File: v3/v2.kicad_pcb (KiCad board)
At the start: 2 copper layers, 178.7 x 150.8 mm, 122 parts, among them J2 Conn_01x04_Pin, J3 Conn_01x04_Pin, SW1 SW_Push, SW10 SW_Push, SW11 SW_Push, SW12 SW_Push, SW13 SW_Push, SW14 SW_Push, SW15 SW_Push, SW16 SW_Push, SW17 SW_Push, SW18 SW_Push, SW19 SW_Push, SW2 SW_Push, SW20 SW_Push, SW21 SW_Push, SW22 SW_Push, SW23 SW_Push, SW24 SW_Push, SW25 SW_Push, SW26 SW_Push, SW27 SW_Push, SW28 SW_Push, SW29 SW_Push, SW3 SW_Push, SW30 SW_Push, SW31 SW_Push, SW32 SW_Push, SW33 RotaryEncoder_Switch, SW4 SW_Push, SW5 SW_Push, SW6 SW_Push, SW7 SW_Push, SW8 SW_Push, SW9 SW_Push, U1 Pico, U2 Pico

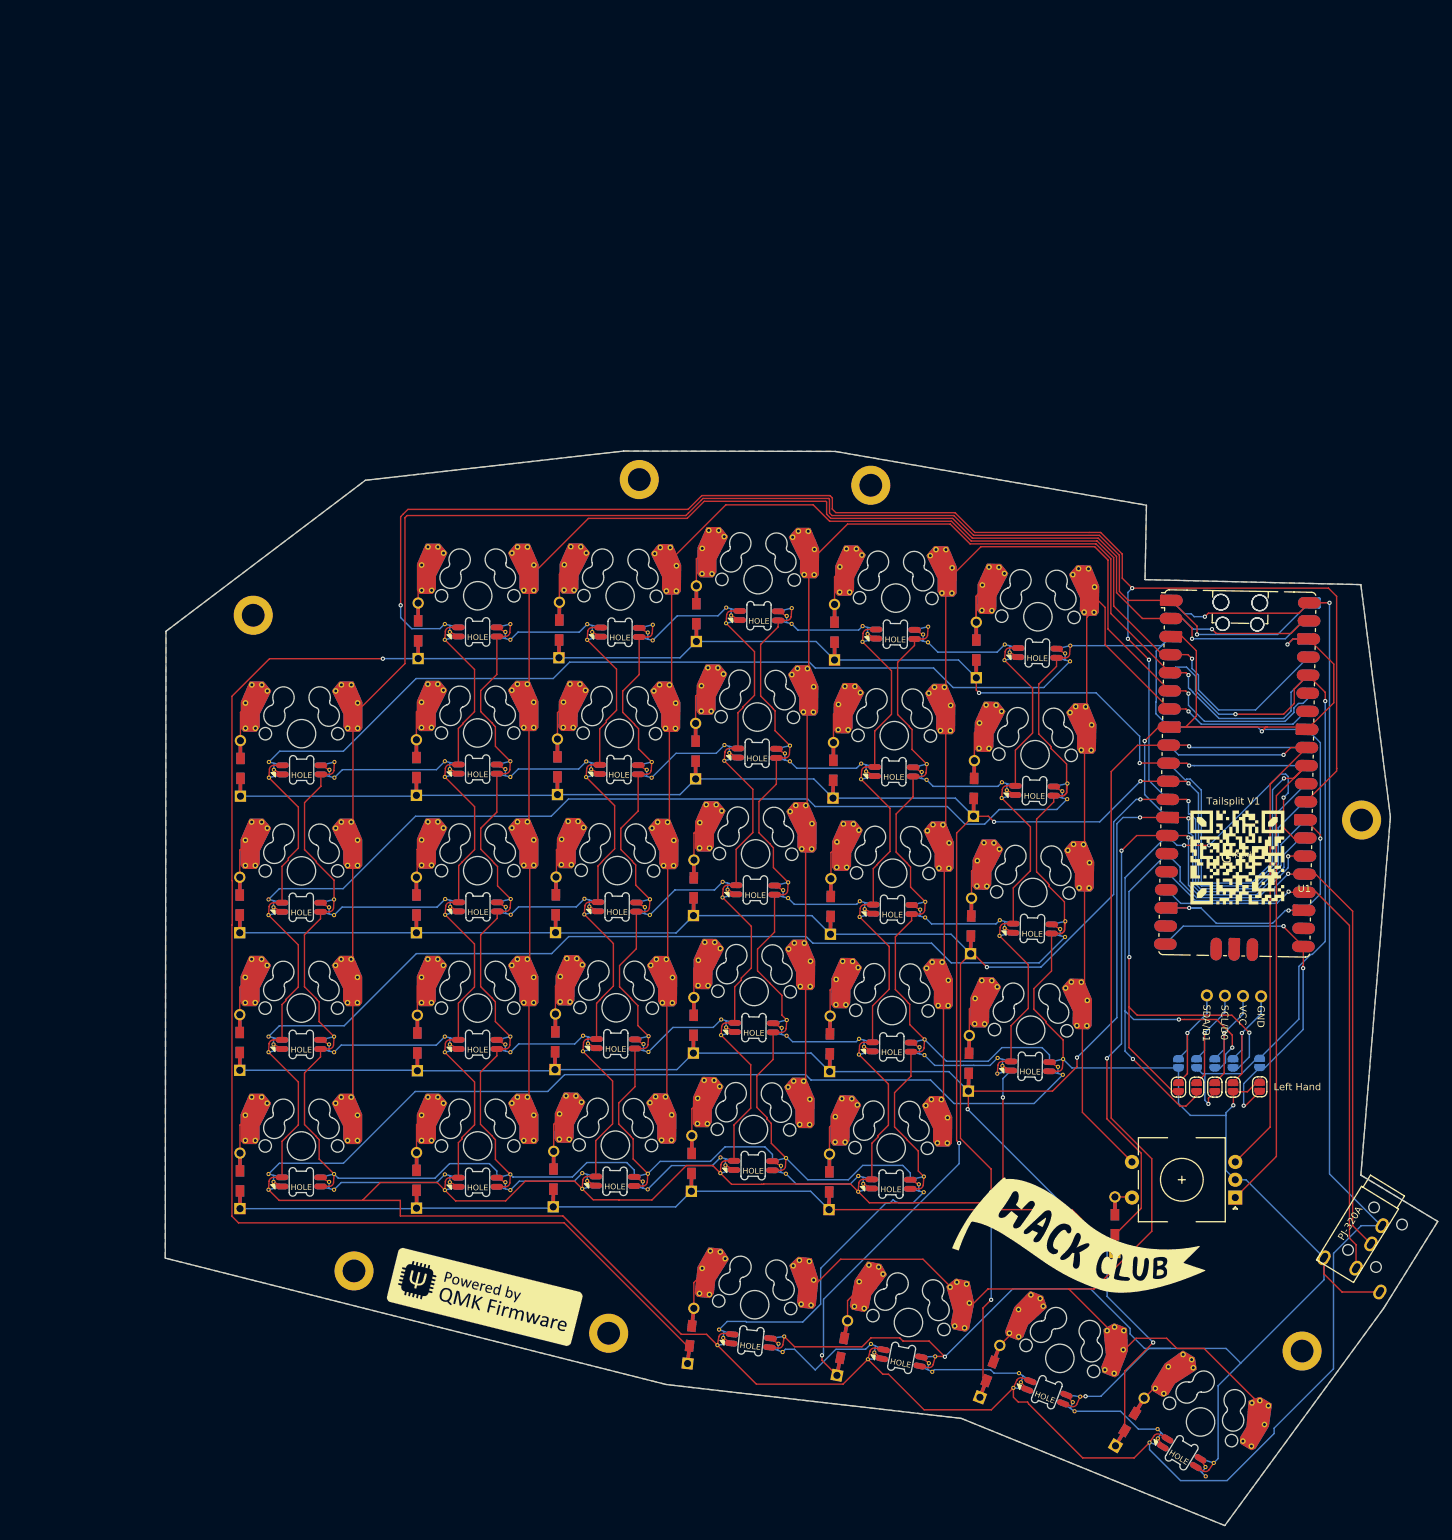
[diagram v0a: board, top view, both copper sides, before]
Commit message: redid footprints and layout for pcb
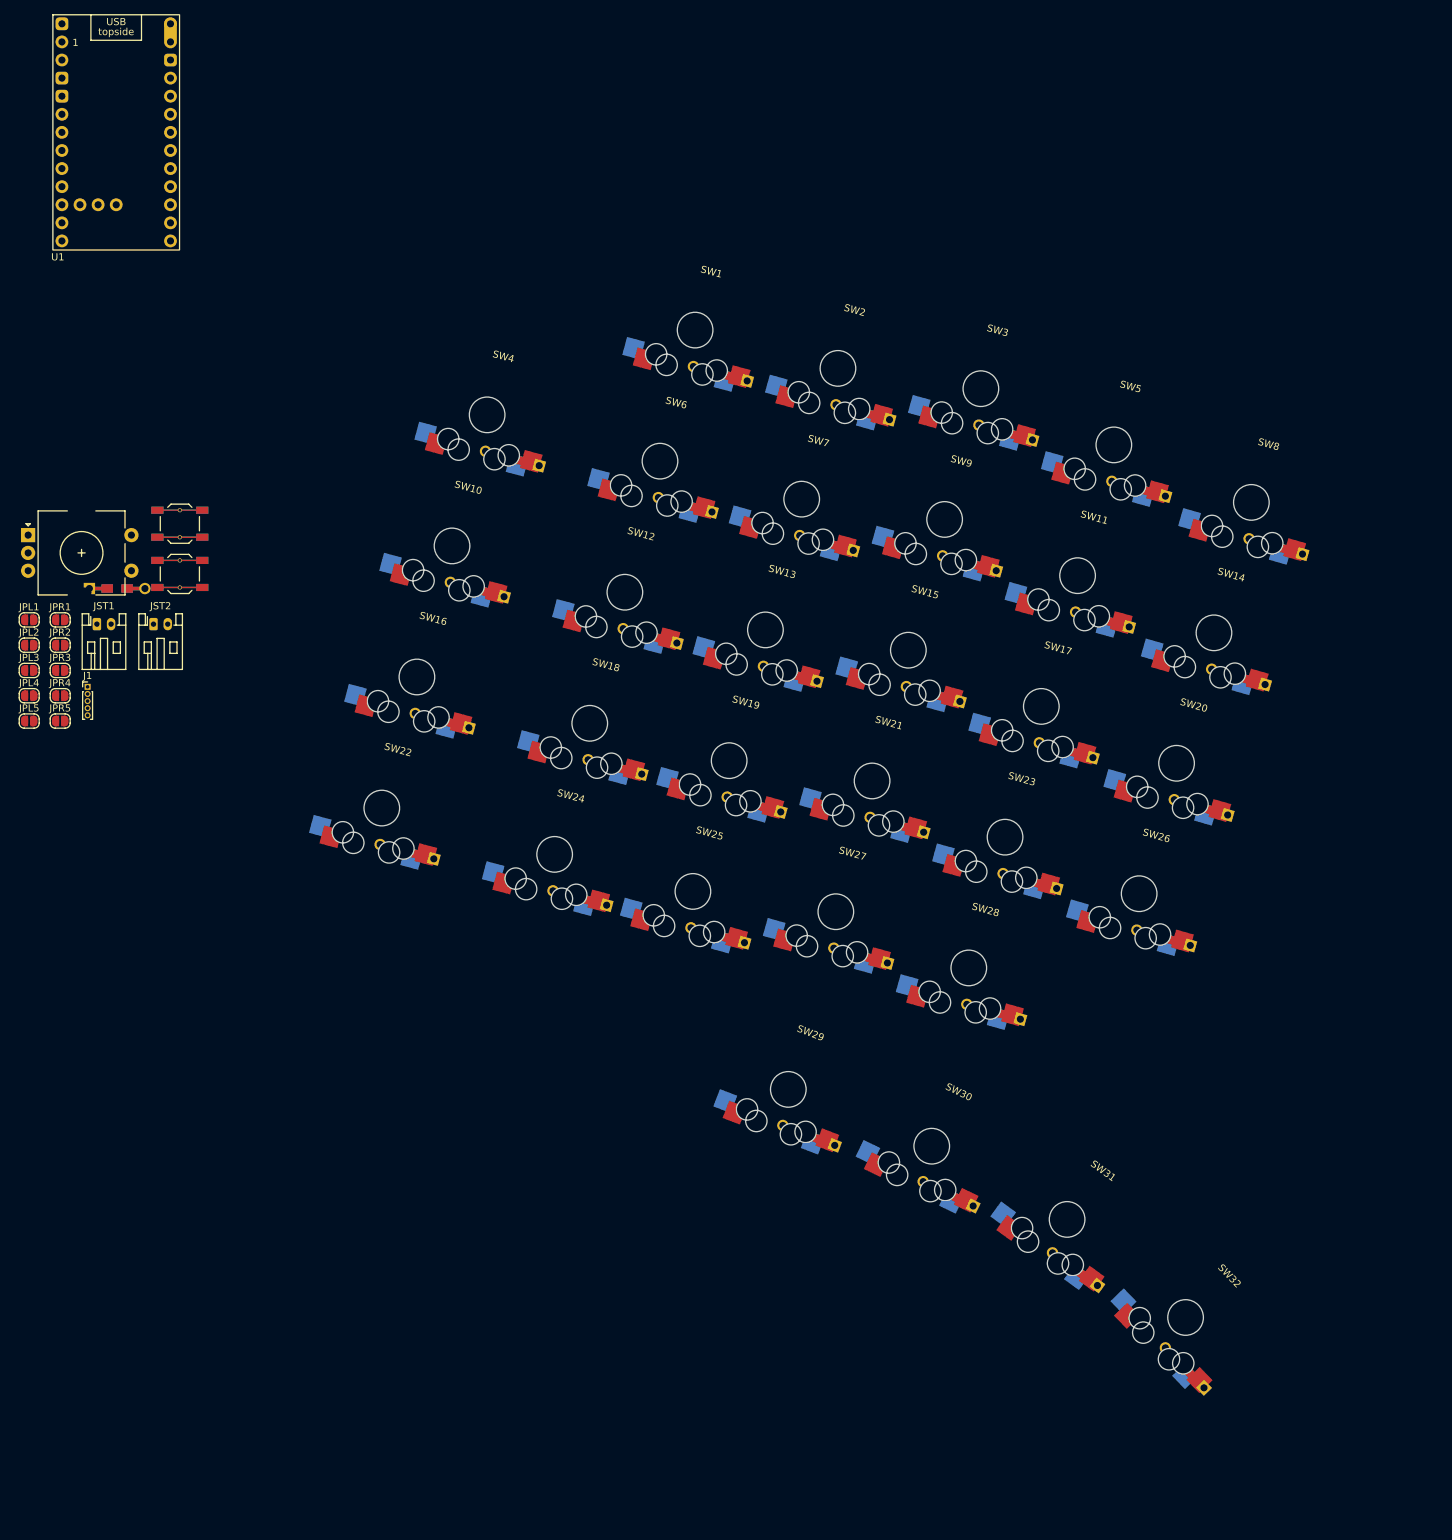
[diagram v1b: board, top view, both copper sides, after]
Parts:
- removed G*** (x2): LOGO, footprints:QMK_PoweredBy
- removed G***: LOGO, LOGO
- removed J2: Conn_01x04_Pin, Keebio-Parts:I2C_Breakout
- removed J3: Conn_01x04_Pin, Keebio-Parts:TRRS-PJ-320A-dual
- removed JP1, JP8: GND, Jumper:SolderJumper-2_P1.3mm_Open_RoundedPad1.0x1.5mm
- removed JP10: Left, Jumper:SolderJumper-2_P1.3mm_Open_RoundedPad1.0x1.5mm
- removed JP2, JP7: VCC, Jumper:SolderJumper-2_P1.3mm_Open_RoundedPad1.0x1.5mm
- removed JP3, JP6: SCL, Jumper:SolderJumper-2_P1.3mm_Open_RoundedPad1.0x1.5mm
- removed JP4, JP5: SDA, Jumper:SolderJumper-2_P1.3mm_Open_RoundedPad1.0x1.5mm
- removed JP9: Right, Jumper:SolderJumper-2_P1.3mm_Open_RoundedPad1.0x1.5mm
- removed LED1, LED10, LED11, LED12, LED13, LED14, LED15, LED16, LED17, LED18, LED19, LED2, LED20, LED21, LED22, LED23, LED24, LED25, LED26, LED27, LED28, LED29, LED3, LED30, LED31, LED32, LED4, LED5, LED6, LED7, LED8, LED9: SK6812MINI, reversible-kicad-footprints:MX-1U-SK6812Mini-E
- removed REF** (x7): MountingHole_3.2mm_M3_ISO14580_Pad, Keebio-Parts:MountingHole_3.2mm_M3_ISO14580_Pad
- removed U2: Pico, Module:RaspberryPi_Pico_SMD_HandSolder
- added J1: Conn_01x05_Pin, Connector_PinHeader_1.00mm:PinHeader_1x05_P1.00mm_Vertical, F.Cu at (96.2, 109.8)
- added JPL1: SolderJumper_2_Open, Jumper:SolderJumper-2_P1.3mm_Open_RoundedPad1.0x1.5mm, F.Cu at (88.0, 100.5)
- added JPL2: SolderJumper_2_Open, Jumper:SolderJumper-2_P1.3mm_Open_RoundedPad1.0x1.5mm, F.Cu at (88.0, 104.0)
- added JPL3: SolderJumper_2_Open, Jumper:SolderJumper-2_P1.3mm_Open_RoundedPad1.0x1.5mm, F.Cu at (88.0, 107.5)
- added JPL4: SolderJumper_2_Open, Jumper:SolderJumper-2_P1.3mm_Open_RoundedPad1.0x1.5mm, F.Cu at (88.0, 111.1)
- added JPL5: SolderJumper_2_Open, Jumper:SolderJumper-2_P1.3mm_Open_RoundedPad1.0x1.5mm, F.Cu at (88.0, 114.7)
- added JPR1: SolderJumper_2_Open, Jumper:SolderJumper-2_P1.3mm_Open_RoundedPad1.0x1.5mm, F.Cu at (92.4, 100.5)
- added JPR2: SolderJumper_2_Open, Jumper:SolderJumper-2_P1.3mm_Open_RoundedPad1.0x1.5mm, F.Cu at (92.4, 104.0)
- added JPR3: SolderJumper_2_Open, Jumper:SolderJumper-2_P1.3mm_Open_RoundedPad1.0x1.5mm, F.Cu at (92.4, 107.5)
- added JPR4: SolderJumper_2_Open, Jumper:SolderJumper-2_P1.3mm_Open_RoundedPad1.0x1.5mm, F.Cu at (92.4, 111.1)
- added JPR5: SolderJumper_2_Open, Jumper:SolderJumper-2_P1.3mm_Open_RoundedPad1.0x1.5mm, F.Cu at (92.4, 114.7)
- added JST1: Conn_01x02_Pin, Connector_JST:JST_PH_S2B-PH-K_1x02_P2.00mm_Horizontal, F.Cu at (97.5, 101.0)
- added JST2: Conn_01x02_Pin, Connector_JST:JST_PH_S2B-PH-K_1x02_P2.00mm_Horizontal, F.Cu at (105.5, 101.0)
- added PWR1: SW_Push_45deg, reversible-kicad-footprints:SMD_Push, F.Cu at (109.2, 87.0)
- added RST1: SW_Push_45deg, reversible-kicad-footprints:SMD_Push, F.Cu at (109.2, 94.0)
- D1, D10, D11, D12, D13, D14, D15, D16, D17, D18, D19, D2, D20, D21, D22, D23, D24, D25, D26, D27, D28, D29, D3, D30, D31, D32, D33, D4, D5, D6, D7, D8, D9: footprint Keebio-Parts:Diode-Hybrid-Dual -> footprints:Diode-dual; moved to B.Cu
- SW1, SW10, SW11, SW12, SW13, SW14, SW15, SW16, SW17, SW18, SW19, SW2, SW20, SW21, SW22, SW23, SW24, SW25, SW26, SW27, SW28, SW29, SW3, SW30, SW31, SW32, SW4, SW5, SW6, SW7, SW8, SW9: footprint reversible-kicad-footprints:MX-1U-Hotswap -> footprints:gateron-ks27-hotswap-reversible
- SW33: footprint Keebio-Parts:RotaryEncoder_EC11 -> Keebio-Parts.pretty-master:RotaryEncoder_EC11
- U1: value Pico -> nice_nano; footprint Module:RaspberryPi_Pico_SMD_HandSolder -> PCM_marbastlib-xp-promicroish:nice_nano_AH_USBup
- moved U1 180.7 mm to (100.3, 33.3), turned to 0 degrees
- moved SW33 177.8 mm to (95.4, 91.0), turned to 0 degrees
- moved D8 153.9 mm to (263.1, 90.1), turned to -16 degrees
- moved SW8 143.0 mm to (259.6, 84.0), turned to -16 degrees
- moved SW7 113.3 mm to (196.5, 83.5), turned to -15.5 degrees
- moved D7 112.9 mm to (200.0, 89.7), turned to -15.5 degrees
- moved D14 109.4 mm to (257.8, 108.5), turned to -16 degrees
- moved D15 108.9 mm to (215.0, 110.9), turned to -15.5 degrees
- moved SW14 105.9 mm to (254.4, 102.3), turned to -16 degrees
- moved SW15 98.9 mm to (211.5, 104.7), turned to -15.5 degrees
- moved D29 93.1 mm to (100.4, 96.0), turned to 180 degrees
- moved D23 88.9 mm to (228.5, 137.1), turned to -15.5 degrees
- moved D1 87.2 mm to (185.1, 65.9), turned to -15 degrees
- moved SW21 85.2 mm to (206.4, 123.1), turned to -15.5 degrees
- moved D9 82.8 mm to (220.0, 92.5), turned to -15.5 degrees
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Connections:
- D1 pad 1: Row 2 -> Row 1
- D12 pad 1: Row 2 -> Row 3
- D13 pad 1: Row 2 -> Row 3
- D14 pad 1: Row 2 -> Row 3
- D15 pad 1: Row 4 -> Row 3
- D18 pad 1: Row 3 -> Row 4
- D19 pad 1: Row 3 -> Row 4
- D20 pad 1: Row 3 -> Row 4
- D21 pad 1: Row 3 -> Row 4
- D22 pad 1: Row 5 -> Row 4
- D24 pad 1: Row 4 -> Row 5
- D25 pad 1: Row 4 -> Row 5
- D26 pad 1: Row 4 -> Row 5
- D27 pad 1: Row 4 -> Row 5
- D28 pad 1: Row 4 -> Row 5
- D29 pad 2: Net-(D29-A) -> ENCSWB
- D30 pad 1: Row 5 -> Row 6
- D31 pad 1: Row 5 -> Row 6
- D32 pad 1: Row 5 -> Row 6
- D33 pad 1: Row 5 -> Row 6
- D33 pad 2: ENCSWB -> Net-(D33-A)
- D6 pad 1: Row 1 -> Row 2
- D7 pad 1: Row 1 -> Row 2
- D8 pad 1: Row 3 -> Row 2
- SW1 pad 2: Col 1 -> Col 2
- SW10 pad 2: Col 3 -> Col 5
- SW11 pad 2: Col 4 -> Col 6
- SW12 pad 2: Col 5 -> Col 1
- SW13 pad 2: Col 6 -> Col 2
- SW14 pad 2: Col 7 -> Col 3
- SW15 pad 2: Col 1 -> Col 4
- SW16 pad 2: Col 2 -> Col 5
- SW17 pad 2: Col 3 -> Col 6
- SW18 pad 2: Col 4 -> Col 1
- SW19 pad 2: Col 5 -> Col 2
- SW2 pad 2: Col 2 -> Col 3
- SW20 pad 2: Col 6 -> Col 3
- SW21 pad 2: Col 7 -> Col 4
- SW22 pad 2: Col 1 -> Col 5
- SW23 pad 2: Col 2 -> Col 6
- SW24 pad 2: Col 3 -> Col 1
- SW25 pad 2: Col 4 -> Col 2
- SW26 pad 2: Col 5 -> Col 3
- SW27 pad 2: Col 6 -> Col 4
- SW28 pad 2: Col 7 -> Col 5
- SW29 pad 1: Net-(D29-A) -> Net-(D30-A)
- SW29 pad 2: Col 2 -> Col 1
- SW3 pad 2: Col 3 -> Col 4
- SW30 pad 1: Net-(D30-A) -> Net-(D31-A)
- SW30 pad 2: Col 3 -> Col 2
- SW31 pad 1: Net-(D31-A) -> Net-(D32-A)
- SW31 pad 2: Col 4 -> Col 3
- SW32 pad 1: Net-(D32-A) -> Net-(D33-A)
- SW32 pad 2: Col 5 -> Col 4
- SW4 pad 2: Col 4 -> Col 5
- SW5 pad 2: Col 5 -> Col 6
- SW6 pad 2: Col 6 -> Col 1
- SW7 pad 2: Col 7 -> Col 2
- SW8 pad 2: Col 1 -> Col 3
- SW9 pad 2: Col 2 -> Col 4
- U1 pad 1: Col 1 -> unconnected-(U1-P0.06-Pad1)
- U1 pad 10: Row 1 -> unconnected-(U1-P0.11-Pad10)
- U1 pad 11: Row 2 -> unconnected-(U1-P1.04-LF-Pad11)
- U1 pad 12: Row 3 -> unconnected-(U1-P1.06-LF-Pad12)
- U1 pad 13: Row 4 -> unconnected-(U1-BAT+-Pad13)
- U1 pad 14: Row 5 -> unconnected-(U1-GND-Pad14)
- U1 pad 18: GND -> unconnected-(U1-P0.29-LF-Pad18)
- U1 pad 2: Col 2 -> unconnected-(U1-P0.08-Pad2)
- U1 pad 21: SPLIT SELECT -> unconnected-(U1-P1.13-LF-Pad21)
- U1 pad 23: GND -> unconnected-(U1-P0.10-LF-Pad23)
- U1 pad 24: SERIAL B -> unconnected-(U1-P0.09-LF-Pad24)
- U1 pad 25: SERIAL A -> unconnected-(U1-P1.01-LF-Pad25)
- U1 pad 26: SDA -> unconnected-(U1-P1.02-LF-Pad26)
- U1 pad 27: SDL -> unconnected-(U1-P1.07-LF-Pad27)
- U1 pad 28: GND -> unconnected-(U1-GND-Pad28)
- U1 pad 29: SK6912PWM -> unconnected-(U1-BAT+-Pad29)
- U1 pad 3: GND -> unconnected-(U1-GND-Pad3)
- U1 pad 4: Col 3 -> unconnected-(U1-GND-Pad4)
- U1 pad 5: Col 4 -> unconnected-(U1-P0.17-Pad5)
- U1 pad 6: Col 5 -> unconnected-(U1-P0.20-Pad6)
- U1 pad 7: Col 6 -> unconnected-(U1-P0.22-Pad7)
- U1 pad 8: GND -> unconnected-(U1-P0.24-Pad8)
- U1 pad 9: Col 7 -> unconnected-(U1-P1.00-Pad9)
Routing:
- net GND: track 943.5 -> 0.00 mm, vias 9 -> 0
- net VBUS: track 883.7 -> 0.00 mm, vias 3 -> 0
- net Row 1: track 309.3 -> 0.00 mm, vias 4 -> 0
- net Row 2: track 267.3 -> 0.00 mm, vias 5 -> 0
- net Row 4: track 261.2 -> 0.00 mm, vias 5 -> 0
- net Row 3: track 252.0 -> 0.00 mm, vias 5 -> 0
- net Col 1: track 231.3 -> 0.00 mm, vias 1 -> 0
- net SK6912PWM: track 225.6 -> 0.00 mm, vias 4 -> 0
- net Row 5: track 224.1 -> 0.00 mm, vias 3 -> 0
- net Col 2: track 205.2 -> 0.00 mm, vias 1 -> 0
- net Col 7: track 197.5 -> 0.00 mm, vias 1 -> 0
- net Col 3: track 192.1 -> 0.00 mm, vias 1 -> 0
- net Col 4: track 170.6 -> 0.00 mm, vias 1 -> 0
- net Col 5: track 149.3 -> 0.00 mm, vias 1 -> 0
- net Col 6: track 123.9 -> 0.00 mm, vias 1 -> 0
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- removed copper zone on B.Cu, net GND
- removed copper zone on F.Cu, net GND
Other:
- board outline removed
- board text removed: "Left Hand"
- board text removed: "Right Hand"
- board text removed: "Tailsplit V1"

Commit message: start placing switches
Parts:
- J1: footprint Connector_PinHeader_1.00mm:PinHeader_1x05_P1.00mm_Vertical -> Connector_PinHeader_2.54mm:PinHeader_1x05_P2.54mm_Vertical
- PWR1, RST1: footprint reversible-kicad-footprints:SMD_Push -> footprints:EVQ-P7C-Reversible
- moved D16 76.2 mm to (149.1, 190.7)
- moved D10 76.2 mm to (154.0, 172.3)
- moved D18 76.2 mm to (173.4, 197.2)
- moved D22 76.2 mm to (144.2, 209.1)
- moved D24 76.2 mm to (168.4, 215.6)
- moved D6 76.2 mm to (183.2, 160.4)
- moved D1 76.2 mm to (188.2, 142.0)
- moved D12 76.2 mm to (178.3, 178.8)
- moved D4 76.2 mm to (159.0, 153.9)
- moved D13 76.2 mm to (198.0, 184.1)
- moved D15 76.2 mm to (218.0, 187.0)
- moved D17 76.2 mm to (236.7, 194.9)
- moved D19 76.2 mm to (192.9, 202.5)
- moved D23 76.2 mm to (231.6, 213.2)
- moved D25 76.2 mm to (187.8, 220.8)
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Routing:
- net Net-(D31-A): track 0.00 -> 3.87 mm
- net Net-(D15-A): track 0.00 -> 3.87 mm
- net Net-(D9-A): track 0.00 -> 3.87 mm
- net Net-(D5-A): track 0.00 -> 3.87 mm
- net Net-(D3-A): track 0.00 -> 3.87 mm
- net Net-(D2-A): track 0.00 -> 3.87 mm
- net Net-(D32-A): track 0.00 -> 3.87 mm
- net Net-(D33-A): track 0.00 -> 3.87 mm
- net Net-(D23-A): track 0.00 -> 3.87 mm
- net Net-(D17-A): track 0.00 -> 3.87 mm
- net Net-(D21-A): track 0.00 -> 3.87 mm
- net Net-(D19-A): track 0.00 -> 3.87 mm
- net Net-(D28-A): track 0.00 -> 3.87 mm
- net Net-(D7-A): track 0.00 -> 3.87 mm
- net Net-(D27-A): track 0.00 -> 3.87 mm
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
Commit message: grid sizing right and other fun stuff
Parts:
- D1, D10, D11, D12, D13, D14, D15, D16, D17, D18, D19, D2, D20, D21, D22, D23, D24, D25, D26, D27, D28, D29, D3, D30, D31, D32, D33, D4, D5, D6, D7, D8, D9: moved to F.Cu
- moved SW8 248.8 mm to (20.9, 134.0), turned to 0 degrees
- moved SW26 247.6 mm to (77.8, 37.4), turned to 0 degrees
- moved SW17 244.3 mm to (58.9, 21.3), turned to 0 degrees
- moved D33 242.1 mm to (113.3, 80.4), turned to 0 degrees
- moved SW5 237.1 mm to (20.9, 85.7), turned to 0 degrees
- moved SW14 235.4 mm to (39.9, 101.8), turned to 0 degrees
- moved SW20 235.0 mm to (58.9, 69.6), turned to 0 degrees
- moved SW11 234.1 mm to (39.9, 53.5), turned to 0 degrees
- moved SW9 231.7 mm to (39.9, 21.3), turned to 0 degrees
- moved SW32 228.0 mm to (77.8, 134.0), turned to 0 degrees
- moved D32 225.1 mm to (113.3, 77.7), turned to 0 degrees
- moved SW25 221.5 mm to (77.8, 21.3), turned to 0 degrees
- moved SW31 216.5 mm to (77.8, 117.9), turned to 0 degrees
- moved SW28 215.3 mm to (77.8, 69.6), turned to 0 degrees
- moved D26 210.3 mm to (113.3, 61.7), turned to 0 degrees
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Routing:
- net Net-(D31-A): track 3.87 -> 0.00 mm
- net Net-(D15-A): track 3.87 -> 0.00 mm
- net Net-(D9-A): track 3.87 -> 0.00 mm
- net Net-(D5-A): track 3.87 -> 0.00 mm
- net Net-(D3-A): track 3.87 -> 0.00 mm
- net Net-(D2-A): track 3.87 -> 0.00 mm
- net Net-(D32-A): track 3.87 -> 0.00 mm
- net Net-(D33-A): track 3.87 -> 0.00 mm
- net Net-(D23-A): track 3.87 -> 0.00 mm
- net Net-(D17-A): track 3.87 -> 0.00 mm
- net Net-(D21-A): track 3.87 -> 0.00 mm
- net Net-(D19-A): track 3.87 -> 0.00 mm
- net Net-(D28-A): track 3.87 -> 0.00 mm
- net Net-(D7-A): track 3.87 -> 0.00 mm
- net Net-(D27-A): track 3.87 -> 0.00 mm
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
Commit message: added all needed labels
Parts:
- added U2: nice_nano_right, PCM_marbastlib-xp-promicroish:nice_nano_AH_USBup, B.Cu at (2.52, 33.9)
- U1: value nice_nano -> nice_nano_left
- moved SW5 227.4 mm to (246.1, 53.7), turned to -0.9 degrees
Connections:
- U1 pad 1: unconnected-(U1-P0.06-Pad1) -> CS
- U1 pad 10: unconnected-(U1-P0.11-Pad10) -> Col 5
- U1 pad 11: unconnected-(U1-P1.04-LF-Pad11) -> Col 6
- U1 pad 12: unconnected-(U1-P1.06-LF-Pad12) -> ENC A
- U1 pad 13: unconnected-(U1-BAT+-Pad13) -> +BATT
- U1 pad 14: unconnected-(U1-GND-Pad14) -> GND
- U1 pad 15: unconnected-(U1-RST-Pad15) -> RST
- U1 pad 16: unconnected-(U1-3V3-Pad16) -> +3.3V
- U1 pad 17: unconnected-(U1-P0.31-LF-Pad17) -> Row 1
- U1 pad 18: unconnected-(U1-P0.29-LF-Pad18) -> Row 2
- U1 pad 19: unconnected-(U1-P0.02-LF-Pad19) -> Row 3
- U1 pad 2: unconnected-(U1-P0.08-Pad2) -> Col 1
- U1 pad 20: unconnected-(U1-P1.15-LF-Pad20) -> Row 4
- U1 pad 21: unconnected-(U1-P1.13-LF-Pad21) -> Row 5
- U1 pad 22: unconnected-(U1-P1.11-LF-Pad22) -> Row 6
- U1 pad 23: unconnected-(U1-P0.10-LF-Pad23) -> ENC B
- U1 pad 24: unconnected-(U1-P0.09-LF-Pad24) -> PWR
- U1 pad 28: unconnected-(U1-GND-Pad28) -> GND
- U1 pad 29: unconnected-(U1-BAT+-Pad29) -> +BATT
- U1 pad 3: unconnected-(U1-GND-Pad3) -> GND
- U1 pad 4: unconnected-(U1-GND-Pad4) -> GND
- U1 pad 5: unconnected-(U1-P0.17-Pad5) -> SCK
- U1 pad 6: unconnected-(U1-P0.20-Pad6) -> MOSI
- U1 pad 7: unconnected-(U1-P0.22-Pad7) -> Col 2
- U1 pad 8: unconnected-(U1-P0.24-Pad8) -> Col 3
- U1 pad 9: unconnected-(U1-P1.00-Pad9) -> Col 4

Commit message: place keyswitches
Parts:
- moved SW11 206.6 mm to (245.7, 72.0), turned to -1.2 degrees
- moved SW17 198.9 mm to (245.5, 90.1), turned to -1.2 degrees
- moved SW16 191.7 mm to (225.9, 87.5), turned to -0.6 degrees
- moved SW32 190.0 mm to (265.8, 161.6), turned to -30.9 degrees
- moved SW10 188.9 mm to (226.1, 69.2), turned to -0.6 degrees
- moved SW23 186.4 mm to (245.0, 108.3), turned to -1.2 degrees
- moved SW8 179.0 mm to (187.7, 68.9), turned to -0.6 degrees
- moved SW9 173.0 mm to (206.8, 66.5), turned to -0.6 degrees
- moved SW31 172.9 mm to (247.1, 153.0), turned to -21 degrees
- moved SW15 170.1 mm to (206.8, 84.8), turned to -0.6 degrees
- moved SW22 166.9 mm to (225.8, 105.6), turned to -0.6 degrees
- moved SW28 157.5 mm to (225.6, 123.8), turned to -0.6 degrees
- moved SW30 156.3 mm to (227.0, 148.2), turned to -11.1 degrees
- moved SW7 155.0 mm to (168.0, 68.9)
- moved SW21 148.7 mm to (206.6, 103.0), turned to -0.6 degrees
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
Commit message: reversible nice!nano
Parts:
- removed U2: nice_nano_right, PCM_marbastlib-xp-promicroish:nice_nano_AH_USBup
- JPR1, JPR2, JPR3, JPR4, JPR5, JST2: moved to B.Cu
- U1: footprint PCM_marbastlib-xp-promicroish:nice_nano_AH_USBup -> PCM_marbastlib-xp-promicroish:nice_nano_AH_Reversible
- moved JPL5 189.5 mm to (278.0, 94.2), turned to -90 degrees
- moved JPL4 185.6 mm to (274.4, 94.2), turned to -90 degrees
- moved JPR5 185.2 mm to (278.0, 94.2), turned to -90 degrees
- moved PWR1 184.4 mm to (277.9, 144.9), turned to 75 degrees
- moved RST1 182.8 mm to (276.0, 151.6), turned to 75 degrees
- moved JPL3 181.8 mm to (270.9, 94.2), turned to -90 degrees
- moved JPR4 181.3 mm to (274.4, 94.2), turned to -90 degrees
- moved JST1 179.4 mm to (278.1, 108.3), turned to -90 degrees
- moved J1 178.3 mm to (265.8, 89.7), turned to 90 degrees
- moved JPL2 178.1 mm to (267.4, 94.2), turned to -90 degrees
- moved JPR3 177.5 mm to (270.9, 94.2), turned to -90 degrees
- moved JPL1 174.4 mm to (263.8, 94.2), turned to -90 degrees
- moved JPR2 173.7 mm to (267.4, 94.2), turned to -90 degrees
- moved U1 172.8 mm to (270.2, 69.9)
- moved JST2 172.1 mm to (278.1, 116.9), turned to 90 degrees
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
